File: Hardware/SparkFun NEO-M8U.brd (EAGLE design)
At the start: 40.6 x 33 mm, 94 parts, among them J13 U.FL, J2 Qwiic Right Angle, J4 Qwiic Right Angle, U2 3.3V

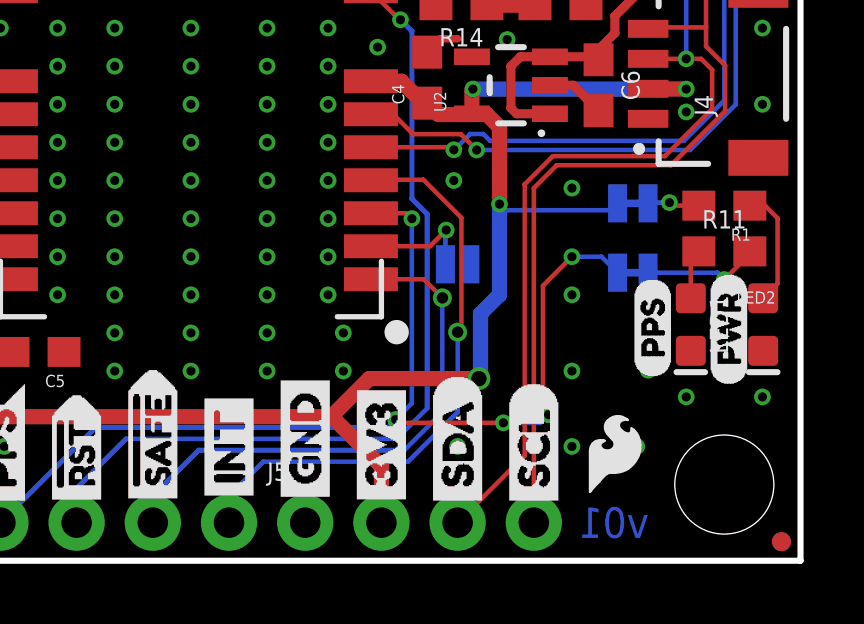
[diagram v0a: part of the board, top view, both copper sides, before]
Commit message: Moves some silk around - resizes some .015 drill hits to .012
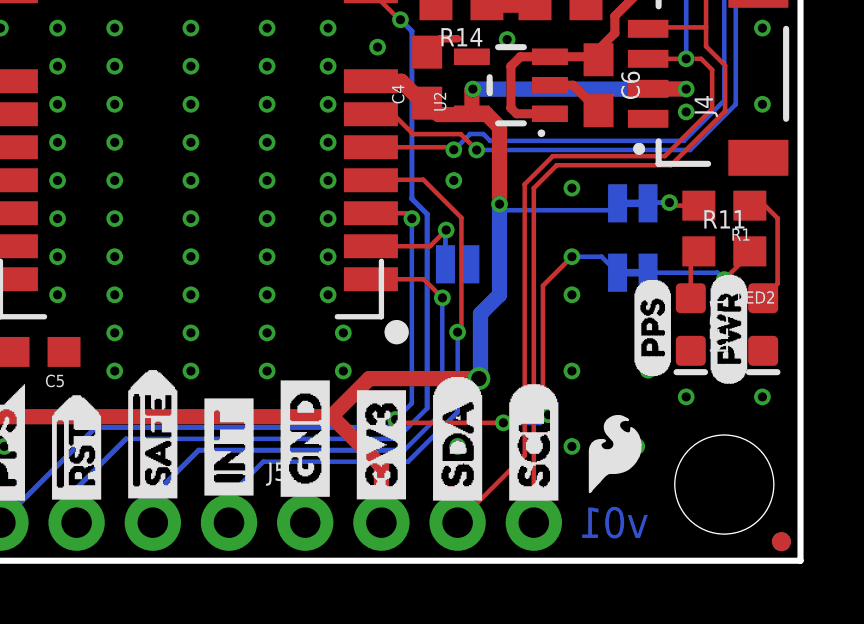
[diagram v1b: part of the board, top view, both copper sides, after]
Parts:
- moved U$11 4.07 mm to (30.6, 11.7)
- moved U$17 3.86 mm to (37.0, 13.7)
- moved U$12 3.70 mm to (36.7, 7.75)
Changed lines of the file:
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@@
 <attribute name="VALUE" x="6.604" y="22.8346" size="0.6096" layer="27" font="vector" ratio="20" rot="R90" align="top-center"/>
 </element>
-<element name="U$11" library="board lables" package="SPI1" value="" x="30.734" y="7.62" smashed="yes" rot="MR0"/>
+<element name="U$11" library="board lables" package="SPI1" value="" x="30.607" y="11.684" smashed="yes" rot="MR0"/>
 <element name="U$14" library="SparkFun-Aesthetics" package="QWIIC_4MM" value="" x="2.54" y="20.4724" smashed="yes"/>
-<element name="U$12" library="LEDs" package="PPS0" value="" x="39.878" y="9.652" smashed="yes" rot="MR0"/>
-<element name="U$17" library="LEDs" package="PWR1" value="" x="40.386" y="11.938" smashed="yes" rot="MR0"/>
+<element name="U$12" library="LEDs" package="PPS0" value="" x="36.703" y="7.747" smashed="yes" rot="MR0"/>
+<element name="U$17" library="LEDs" package="PWR1" value="" x="36.957" y="13.716" smashed="yes" rot="MR0"/>
 <element name="U$21" library="NEO_GPS_board_silk_FINAL#03#jpg" package="NEO_GPS_BOARD_SILK_FINAL#03#JPG" value="" x="15.24" y="11.43" smashed="yes" rot="MR0"/>
 <element name="U$25" library="ANT" package="ANT0" value="" x="34.671" y="20.066" smashed="yes" rot="R90"/>
@@
 <wire x1="19.05" y1="1.27" x2="19.05" y2="2.159" width="0.17" layer="16"/>
 <wire x1="28.702" y1="4.953" x2="28.702" y2="8.763" width="0.1524" layer="16"/>
-<via x="28.702" y="8.763" extent="1-16" drill="0.381"/>
+<via x="28.702" y="8.763" extent="1-16" drill="0.3048"/>
 <wire x1="28.702" y1="8.763" x2="28.082" y2="9.383" width="0.1524" layer="1"/>
 <wire x1="28.082" y1="9.383" x2="26.32" y2="9.383" width="0.1524" layer="1"/>
@@
 <wire x1="22.733" y1="3.302" x2="27.559" y2="3.302" width="0.1524" layer="16"/>
 <wire x1="29.21" y1="4.953" x2="29.21" y2="7.62" width="0.1524" layer="16"/>
-<via x="29.21" y="7.62" extent="1-16" drill="0.381"/>
+<via x="29.21" y="7.62" extent="1-16" drill="0.3048"/>
 <wire x1="29.337" y1="11.43" x2="29.337" y2="7.747" width="0.1524" layer="1"/>
 <wire x1="29.21" y1="7.62" x2="29.337" y2="7.747" width="0.1524" layer="1"/>

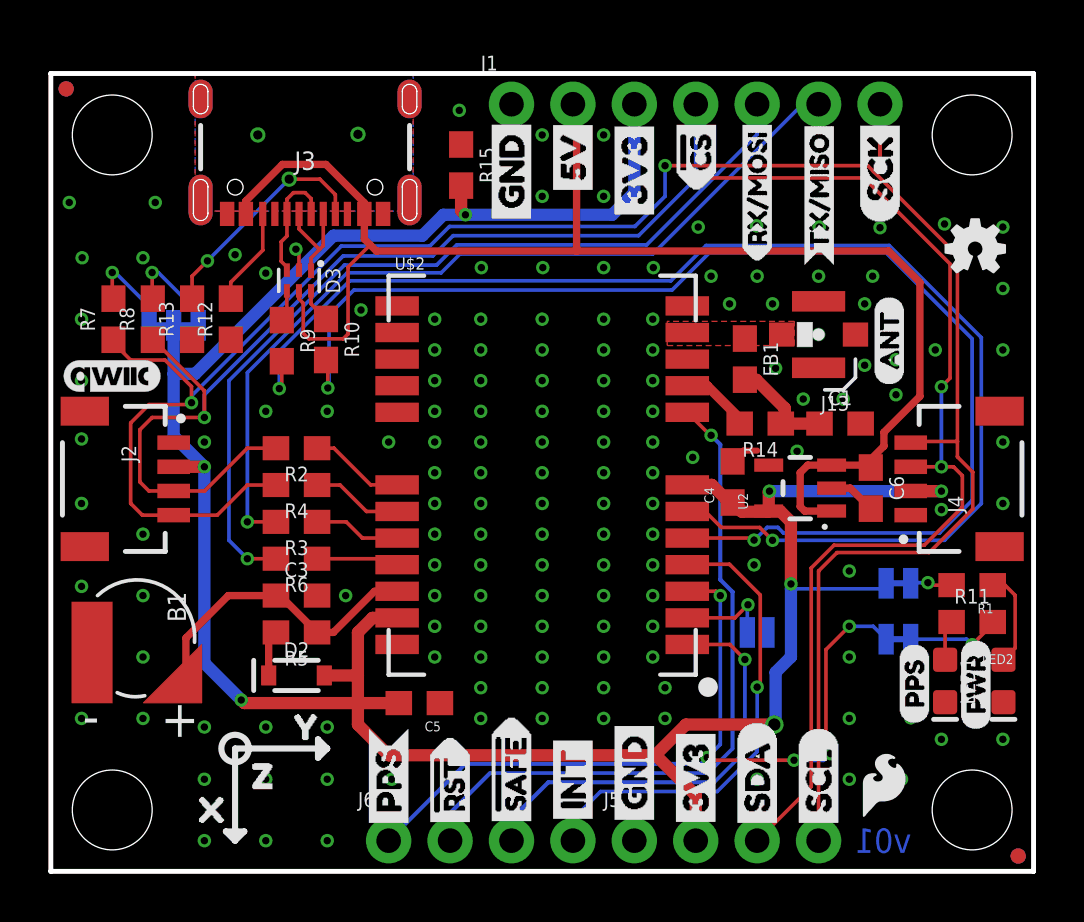
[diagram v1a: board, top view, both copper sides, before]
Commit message: Moves battery circuit around for better aesthetic (heh), adjusts various labels
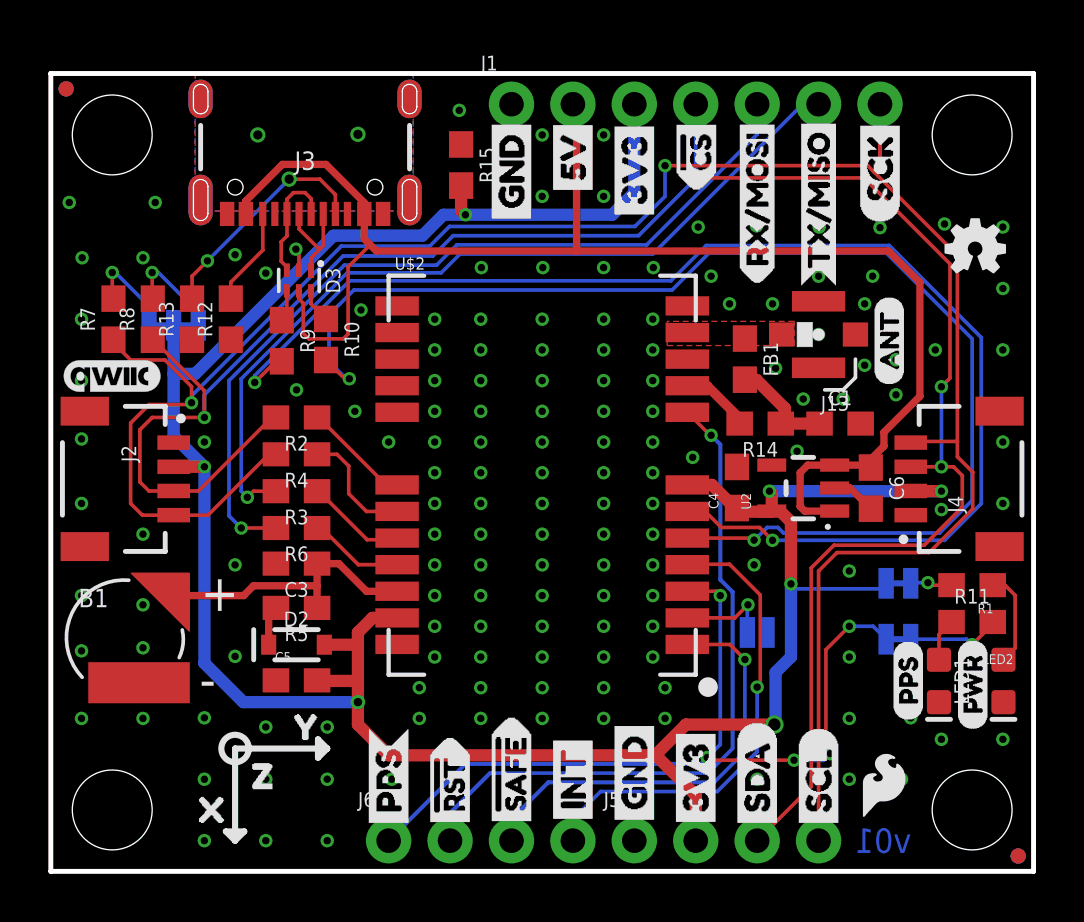
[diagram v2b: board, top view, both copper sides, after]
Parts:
- removed U$34: (no value), buzzard_labels (36):TX#MISO0
- added U$29: (no value), buzzard_labels (36):TX#MISO1
- U$26: device buzzard_labels (36):RX#MOSI2 -> buzzard_labels (36):RX#MOSI3
- moved C5 5.17 mm to (10.2, 7.90), turned to 0 degrees
- moved C3 1.32 mm to (10.2, 12.7), turned to 180 degrees
- moved R2 1.27 mm to (10.2, 18.8)
- moved R4 1.27 mm to (10.2, 17.2)
- moved R6 1.27 mm to (10.2, 14.2)
- moved D2 1.27 mm to (10.2, 9.37)
- moved R3 1.27 mm to (10.2, 15.7)
- moved R5 1.02 mm to (10.2, 10.9)
- moved U$26 0.94 mm to (29.2, 24.2)
- moved B1 0.51 mm to (3.05, 9.65), turned to 0 degrees
- moved C4 0.29 mm to (28.4, 15.9)
- moved U$52 0.28 mm to (35.5, 6.22)
- moved LED1 0.25 mm to (36.7, 7.87)
- moved U$18 0.13 mm to (38.1, 5.84)
- moved U2 0.13 mm to (31.1, 15.8)
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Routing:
- net N$13: track 3.76 -> 6.03 mm
- net GND: track 4.09 -> 2.76 mm, vias 149 -> 153
- net RXI/MOSI: track 36.2 -> 35.0 mm
- net N$3: track 3.94 -> 4.91 mm
- net TXO/MISO: track 35.6 -> 34.9 mm
- net BACKUP: track 12.8 -> 12.2 mm
- net N$15: track 3.59 -> 4.17 mm
- net N$16: track 3.41 -> 3.94 mm
- net SDA/!CS: track 87.3 -> 87.8 mm
- net SCL/SCK: track 90.1 -> 90.6 mm

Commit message: Updates old schematic artifacts, replace power lables with their proper symbols
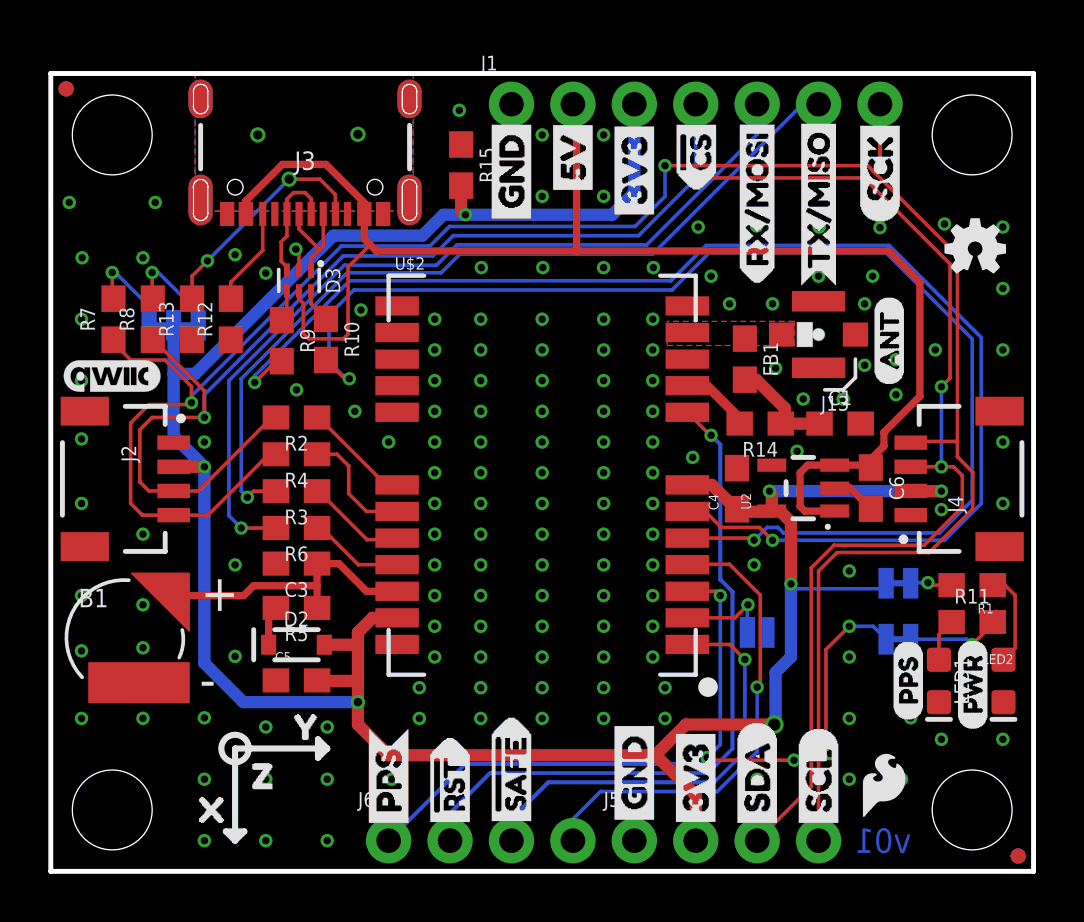
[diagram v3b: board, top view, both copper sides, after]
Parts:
- removed U$15, U$16: (no value), buzzard_labels (5):INT8
- moved C4 0.05 mm to (28.4, 15.8)
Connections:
- net BACKUP renamed V_BATT
- net VCC_RF renamed VDD
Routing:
- net VDD: track 2.94 -> 2.13 mm
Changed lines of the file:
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@@
 <setting verticaltext="up"/>
 </settings>
-<grid distance="0.05" unitdist="inch" unit="inch" style="lines" multiple="1" display="yes" altdistance="0.001" altunitdist="inch" altunit="inch"/>
+<grid distance="0.05" unitdist="inch" unit="inch" style="lines" multiple="1" display="yes" altdistance="0.005" altunitdist="inch" altunit="inch"/>
 <layers>
 <layer number="1" name="Top" color="4" fill="1" visible="yes" active="yes"/>
@@
 <layer number="20" name="Dimension" color="15" fill="1" visible="yes" active="yes"/>
 <layer number="21" name="tPlace" color="16" fill="1" visible="yes" active="yes"/>
-<layer number="22" name="bPlace" color="14" fill="1" visible="no" active="yes"/>
-<layer number="23" name="tOrigins" color="15" fill="1" visible="yes" active="yes"/>
+<layer number="22" name="bPlace" color="14" fill="1" visible="yes" active="yes"/>
+<layer number="23" name="tOrigins" color="15" fill="1" visible="no" active="yes"/>
 <layer number="24" name="bOrigins" color="15" fill="1" visible="yes" active="yes"/>
 <layer number="25" name="tNames" color="7" fill="1" visible="no" active="yes"/>
@@
 <layer number="29" name="tStop" color="7" fill="3" visible="yes" active="yes"/>
 <layer number="30" name="bStop" color="7" fill="6" visible="no" active="yes"/>
-<layer number="31" name="tCream" color="7" fill="4" visible="yes" active="yes"/>
+<layer number="31" name="tCream" color="7" fill="4" visible="no" active="yes"/>
 <layer number="32" name="bCream" color="7" fill="5" visible="no" active="yes"/>
 <layer number="33" name="tFinish" color="6" fill="3" visible="no" active="yes"/>
@@
 <element name="U$9" library="Labels" package="GND-04" value="" x="24.13" y="1.651" smashed="yes" rot="MR90"/>
 <element name="U$10" library="Labels" package="I_SUPER2_C-()-03" value="" x="6.477" y="24.3586" smashed="yes" rot="MR0"/>
-<element name="U$15" library="buzzard_labels (5)" package="INT8" value="" x="21.59" y="1.651" smashed="yes" rot="R90"/>
-<element name="U$16" library="buzzard_labels (5)" package="INT8" value="" x="21.59" y="1.651" smashed="yes" rot="MR90"/>
 <element name="U$22" library="buzzard_labels (5)" package="U#BLOX3" value="" x="24.511" y="18.0086" smashed="yes" rot="MR0"/>
 <element name="U$35" library="buzzard_labels (7)" package="#RST3" value="" x="16.51" y="1.397" smashed="yes" rot="R90"/>
@@
 </element>
 <element name="U$52" library="buzzard_labels (33)" package="PPS0" value="" x="35.4584" y="6.223" smashed="yes" rot="R90"/>
-<element name="C4" library="SparkFun-Capacitors" package="0603" value="1.0uF" x="28.3718" y="15.875" smashed="yes" rot="R90">
-<attribute name="NAME" x="27.6098" y="14.986" size="0.4064" layer="25" font="vector" rot="R90"/>
-<attribute name="PROD_ID" value="CAP-00868" x="28.3718" y="15.875" size="1.778" layer="27" rot="R90" display="off"/>
-<attribute name="VALUE" value="1.0uF" x="28.2448" y="14.478" size="0.4064" layer="27" font="vector" rot="R270"/>
+<element name="C4" library="SparkFun-Capacitors" package="0603" value="1.0uF" x="28.3718" y="15.8242" smashed="yes" rot="R90">
+<attribute name="NAME" x="27.6098" y="14.9352" size="0.4064" layer="25" font="vector" rot="R90"/>
+<attribute name="PROD_ID" value="CAP-00868" x="28.3718" y="15.8242" size="1.778" layer="27" rot="R90" display="off"/>
+<attribute name="VALUE" value="1.0uF" x="28.2448" y="14.4272" size="0.4064" layer="27" font="vector" rot="R270"/>
 </element>
 <element name="C5" library="SparkFun-Capacitors" package="0603" value="0.1uF" x="10.16" y="7.8994" smashed="yes">
@@
 <via x="6.35" y="16.7306" extent="1-16" drill="0.3048"/>
 <wire x1="29.8149" y1="14.8996" x2="29.7879" y2="14.8726" width="0.508" layer="1"/>
-<wire x1="29.7879" y1="14.8726" x2="28.5242" y2="14.8726" width="0.508" layer="1"/>
-<wire x1="28.3718" y1="15.025" x2="28.5242" y2="14.8726" width="0.508" layer="1"/>
+<wire x1="29.7879" y1="14.8726" x2="28.4734" y2="14.8726" width="0.508" layer="1"/>
+<wire x1="28.3718" y1="14.9742" x2="28.4734" y2="14.8726" width="0.508" layer="1"/>
 <wire x1="29.718" y1="15.7226" x2="29.8149" y2="15.6257" width="0.508" layer="1"/>
 <wire x1="29.8149" y1="15.6257" x2="29.8149" y2="14.8996" width="0.508" layer="1"/>
@@
 <contactref element="U$2" pad="7"/>
 <wire x1="13.3024" y1="10.483" x2="14.32" y2="10.483" width="0.508" layer="1"/>
-<wire x1="28.3718" y1="15.025" x2="28.2956" y2="15.025" width="0.508" layer="1"/>
-<wire x1="28.2956" y1="15.025" x2="27.3376" y2="15.983" width="0.508" layer="1"/>
+<wire x1="28.3718" y1="14.9742" x2="28.3464" y2="14.9742" width="0.508" layer="1"/>
+<wire x1="28.3464" y1="14.9742" x2="27.3376" y2="15.983" width="0.508" layer="1"/>
 <wire x1="27.3376" y1="15.983" x2="26.32" y2="15.983" width="0.508" layer="1"/>
 <wire x1="16.9672" y1="27.3304" x2="16.9672" y2="28.36" width="0.508" layer="1"/>
@@
 <wire x1="37.329996875" y1="16.7306" x2="36.83" y2="16.7306" width="0.1524" layer="1"/>
 </signal>
-<signal name="BACKUP">
-<contactref element="C3" pad="1"/>
-<contactref element="B1" pad="+"/>
-<contactref element="R5" pad="1"/>
-<contactref element="U$2" pad="22"/>
-<wire x1="5.07" y1="11.684" x2="5.3494" y2="11.4046" width="0.3048" layer="1"/>
-<wire x1="11.01" y1="10.541" x2="11.01" y2="10.8966" width="0.3048" layer="1"/>
-<wire x1="14.32" y1="11.583" x2="13.055" y2="11.583" width="0.3048" layer="1"/>
-<wire x1="11.9126" y1="12.7254" x2="11.01" y2="12.7254" width="0.3048" layer="1"/>
-<wire x1="13.055" y1="11.583" x2="11.9126" y2="12.7254" width="0.3048" layer="1"/>
-<wire x1="11.01" y1="12.7254" x2="11.01" y2="11.811" width="0.3048" layer="1"/>
-<wire x1="11.01" y1="11.811" x2="11.01" y2="10.8966" width="0.3048" layer="1"/>
-<wire x1="8.382" y1="11.811" x2="11.01" y2="11.811" width="0.3048" layer="1"/>
-<wire x1="5.3494" y1="11.4046" x2="7.9756" y2="11.4046" width="0.3048" layer="1"/>
-<wire x1="7.9756" y1="11.4046" x2="8.382" y2="11.811" width="0.3048" layer="1"/>
-</signal>
 <signal name="PPS">
 <contactref element="PPS" pad="2"/>
@@
 <wire x1="28.829" y1="11.0236" x2="28.2884" y2="10.483" width="0.1524" layer="1"/>
 </signal>
-<signal name="VCC_RF">
-<wire x1="28.487" y1="18.5166" x2="28.487" y2="18.7316" width="0.4064" layer="1"/>
-<wire x1="28.487" y1="18.7316" x2="27.1356" y2="20.083" width="0.4064" layer="1"/>
-<contactref element="R14" pad="2"/>
-<contactref element="U$2" pad="9"/>
-<wire x1="27.1356" y1="20.083" x2="26.32" y2="20.083" width="0.4064" layer="1"/>
-</signal>
 <signal name="ANT_VCC">
 <contactref element="R14" pad="1"/>
@@
 <wire x1="27.559" y1="3.302" x2="29.21" y2="4.953" width="0.1524" layer="16"/>
 </signal>
+<signal name="V_BATT">
+<contactref element="U$2" pad="22"/>
+<contactref element="C3" pad="1"/>
+<contactref element="B1" pad="+"/>
+<contactref element="R5" pad="1"/>
+<wire x1="5.07" y1="11.684" x2="5.3494" y2="11.4046" width="0.3048" layer="1"/>
+<wire x1="11.01" y1="10.541" x2="11.01" y2="10.8966" width="0.3048" layer="1"/>
+<wire x1="11.9126" y1="12.7254" x2="11.01" y2="12.7254" width="0.3048" layer="1"/>
+<wire x1="12.954" y1="11.684" x2="11.9126" y2="12.7254" width="0.3048" layer="1"/>
+<wire x1="11.01" y1="12.7254" x2="11.01" y2="11.811" width="0.3048" layer="1"/>
+<wire x1="11.01" y1="11.811" x2="11.01" y2="10.8966" width="0.3048" layer="1"/>
+<wire x1="8.382" y1="11.811" x2="11.01" y2="11.811" width="0.3048" layer="1"/>
+<wire x1="5.3494" y1="11.4046" x2="7.9756" y2="11.4046" width="0.3048" layer="1"/>
+<wire x1="7.9756" y1="11.4046" x2="8.382" y2="11.811" width="0.3048" layer="1"/>
+<wire x1="14.32" y1="11.583" x2="13.055" y2="11.583" width="0.3048" layer="1"/>
+<wire x1="13.055" y1="11.583" x2="12.954" y2="11.684" width="0.3048" layer="1"/>
+</signal>
+<signal name="VDD">
+<contactref element="U$2" pad="9"/>
+<contactref element="R14" pad="2"/>
+<wire x1="28.487" y1="18.5166" x2="28.487" y2="18.7316" width="0.4064" layer="1"/>
+<wire x1="28.487" y1="18.7316" x2="27.1356" y2="20.083" width="0.4064" layer="1"/>
+<wire x1="27.1356" y1="20.083" x2="26.32" y2="20.083" width="0" layer="19" extent="1-1"/>
+</signal>
 </signals>
